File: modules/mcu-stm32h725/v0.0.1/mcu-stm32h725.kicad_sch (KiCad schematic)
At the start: 38 parts, among them J1 USB-C, J2 Side A, J3 Side B, U1 USB6B1RL, U2 TLV62569DBVR, U3 STM32H725RGV3, U4 TPS2116DRLR, Y1 25MHz

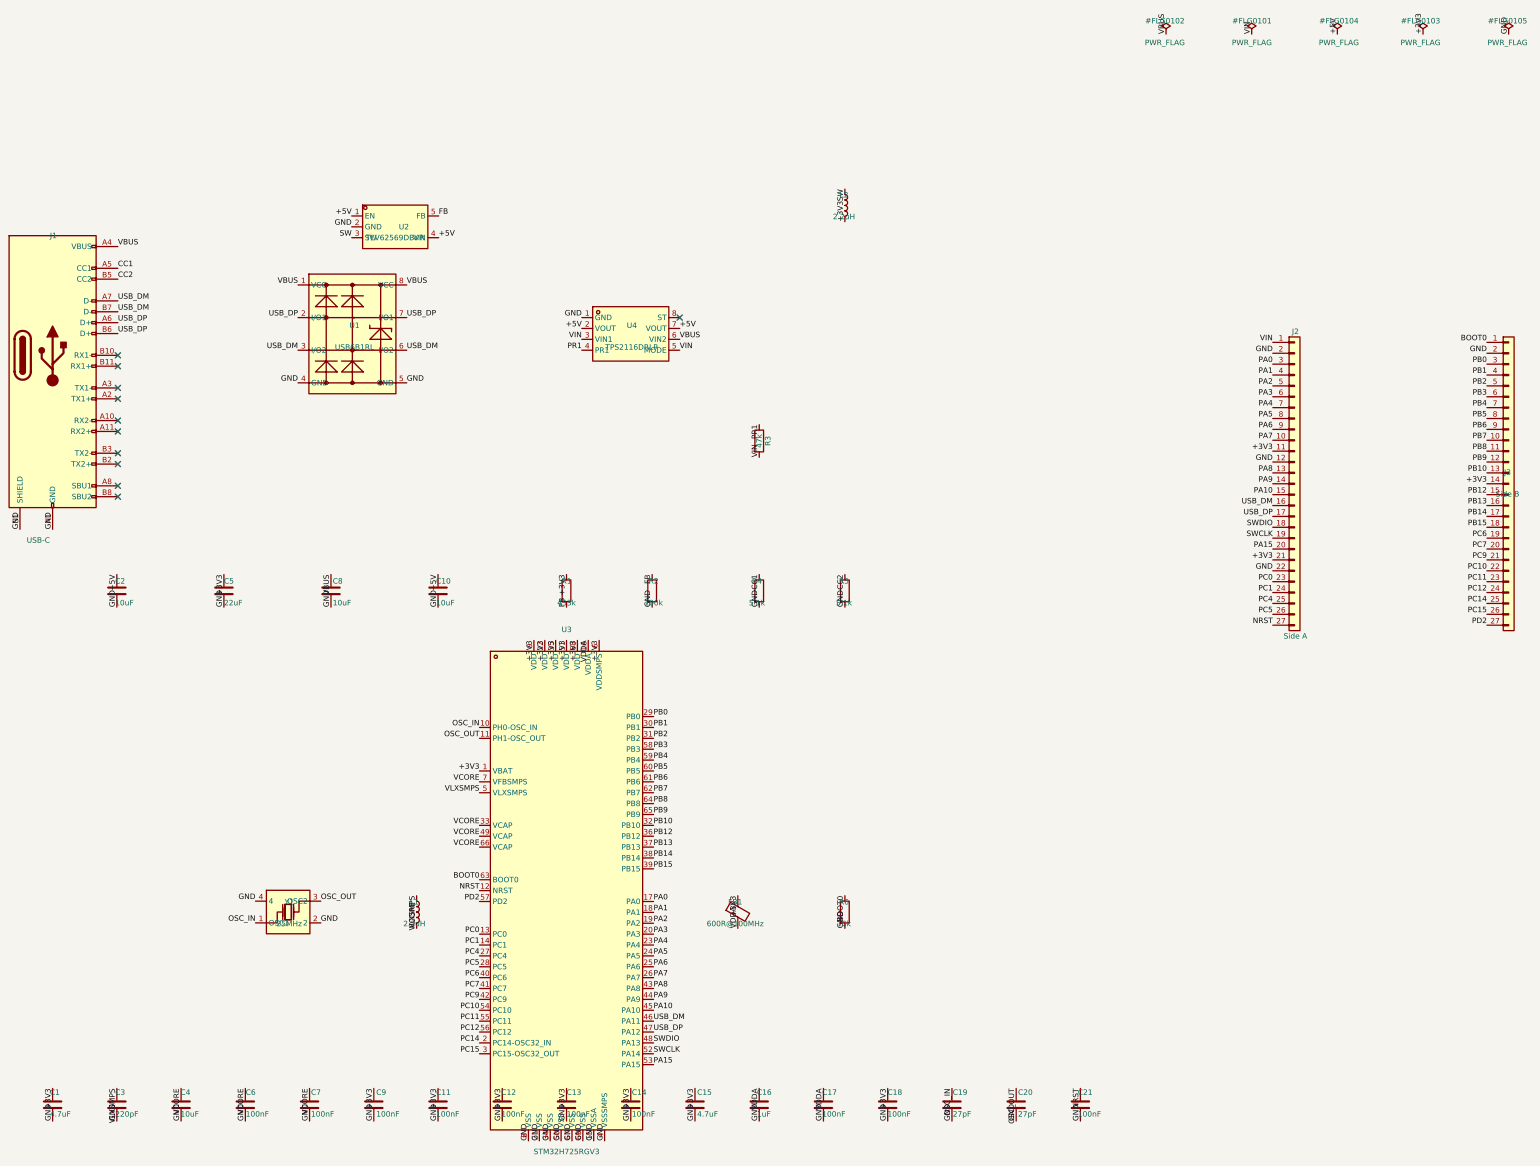
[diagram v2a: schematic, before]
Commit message: Lay out mcu-stm32h725 PCB: centered placement + 4-layer planes + optimal pin map
All 38 footprints placed (MCU centered for balanced GPIO fan-out; power block by USB-C; decoupling ringing the MCU; bulk caps right). GND plane (In1.Cu) + +3V3 plane (In2.Cu) zones added + filled. Castellation pads marked pad_prop_castellated in board + library (clears edge-clearance DRC). Schematic fixes: L1 footprint L_1210_3225Metric; USB-C symbol -> USB_C_Receptacle_USB2.0_16P to match the 16-pad footprint; J1 instance annotation repaired. Castellation pin map is crossing-free per edge and optimal for the centered MCU (~656mm ratsnest). DRC: 0 electrical violations (only unrouted nets + cosmetic silk/fill remain). Routing pending.

Co-Authored-By: Claude Opus 4.8 <noreply@anthropic.com>
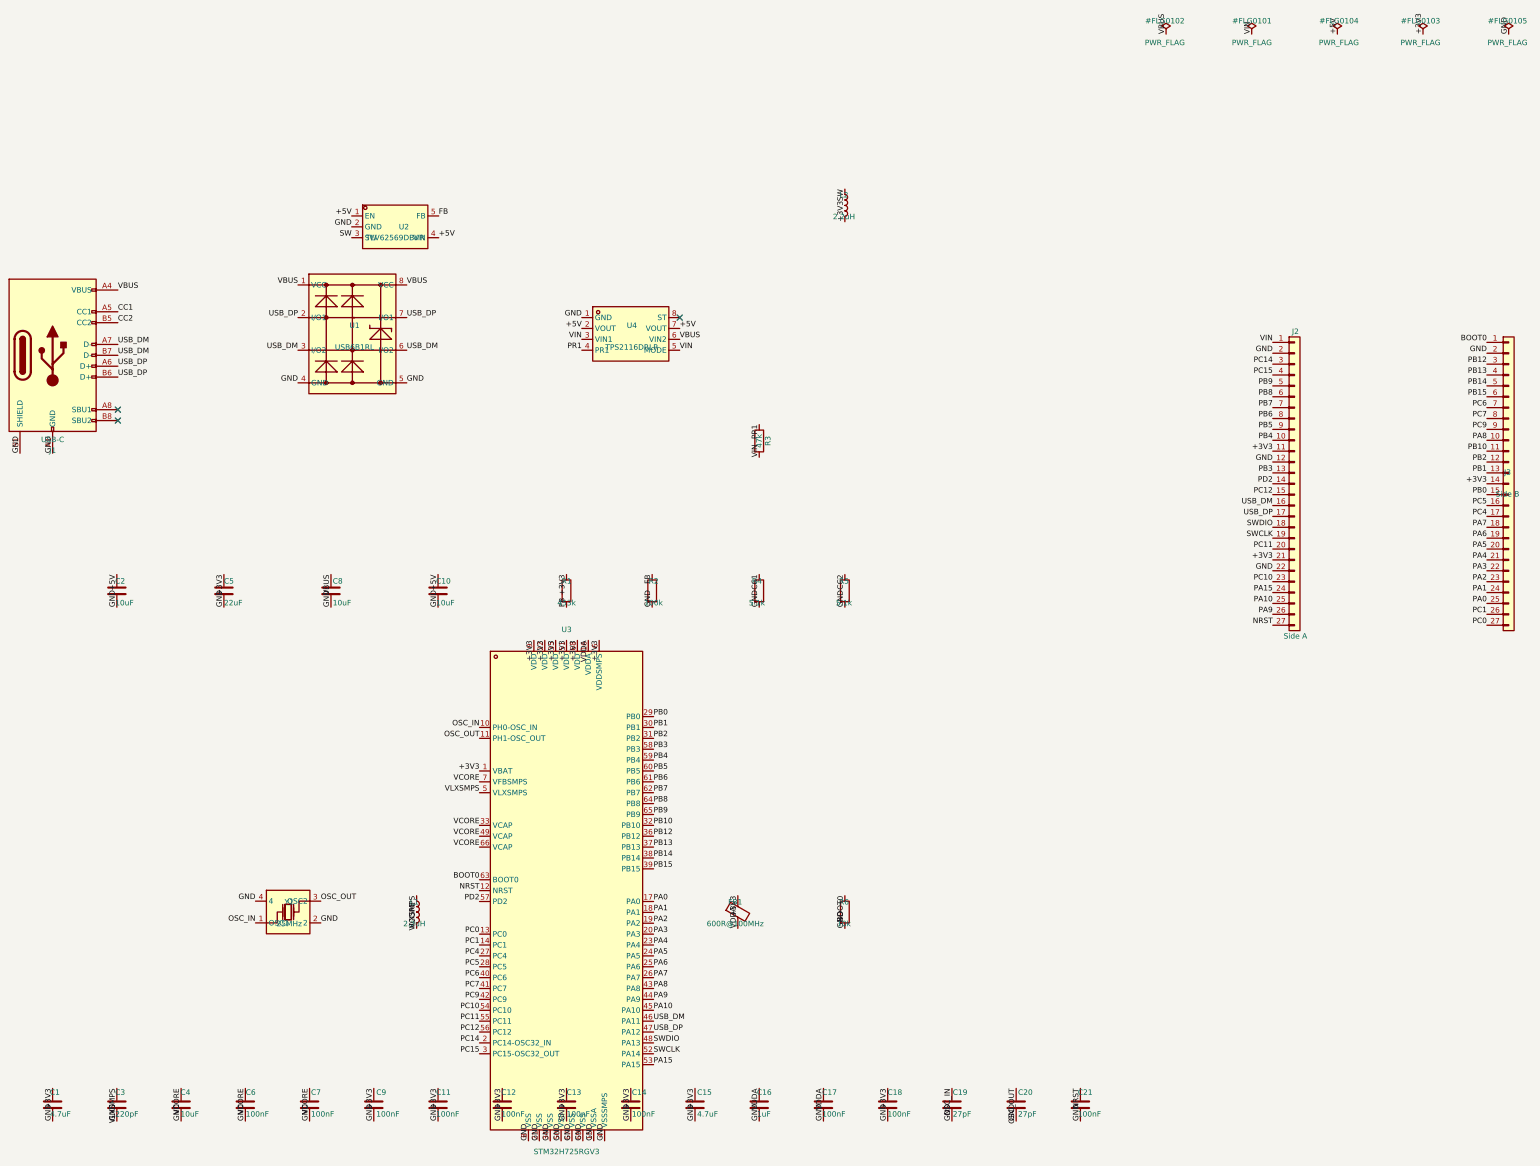
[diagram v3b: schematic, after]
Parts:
- removed J1: USB-C, mcu-stm32h725:USB-C_HYP_TC020-24LB02R_C23376530, symbol Connector:USB_C_Receptacle
- added J1: USB-C, mcu-stm32h725:USB-C_HYP_TC020-24LB02R_C23376530, symbol Connector:USB_C_Receptacle_USB2.0_16P
- L1: footprint Inductor_SMD:L_2520_2520Metric -> Inductor_SMD:L_1210_3225Metric
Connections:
- net CC1: now also J1.A5 (CC1)
- net CC2: now also J1.B5 (CC2)
- net GND: now also J1.A1 (GND), J1.A12 (GND), J1.B1 (GND), J1.B12 (GND), J1.S1 (SHIELD)
- net PA0: now also J3.25 (Pin_25); no longer J2.3 (Pin_3)
- net PA1: now also J3.24 (Pin_24); no longer J2.4 (Pin_4)
- net PA10: now also J2.25 (Pin_25); no longer J2.15 (Pin_15)
- net PA15: now also J2.24 (Pin_24); no longer J2.20 (Pin_20)
- net PA2: now also J3.23 (Pin_23); no longer J2.5 (Pin_5)
- net PA3: now also J3.22 (Pin_22); no longer J2.6 (Pin_6)
- net PA4: now also J3.21 (Pin_21); no longer J2.7 (Pin_7)
- net PA5: now also J3.20 (Pin_20); no longer J2.8 (Pin_8)
- net PA6: now also J3.19 (Pin_19); no longer J2.9 (Pin_9)
- net PA7: now also J3.18 (Pin_18); no longer J2.10 (Pin_10)
- net PA8: now also J3.10 (Pin_10); no longer J2.13 (Pin_13)
- net PA9: now also J2.26 (Pin_26); no longer J2.14 (Pin_14)
- net PB0: now also J3.15 (Pin_15); no longer J3.3 (Pin_3)
- net PB1: now also J3.13 (Pin_13); no longer J3.4 (Pin_4)
- net PB10: now also J3.11 (Pin_11); no longer J3.13 (Pin_13)
- net PB12: now also J3.3 (Pin_3); no longer J3.15 (Pin_15)
- net PB13: now also J3.4 (Pin_4); no longer J3.16 (Pin_16)
- net PB14: now also J3.5 (Pin_5); no longer J3.17 (Pin_17)
- net PB15: now also J3.6 (Pin_6); no longer J3.18 (Pin_18)
- net PB2: now also J3.12 (Pin_12); no longer J3.5 (Pin_5)
- net PB3: now also J2.13 (Pin_13); no longer J3.6 (Pin_6)
- net PB4: now also J2.10 (Pin_10); no longer J3.7 (Pin_7)
- net PB5: now also J2.9 (Pin_9); no longer J3.8 (Pin_8)
- net PB6: now also J2.8 (Pin_8); no longer J3.9 (Pin_9)
- net PB7: now also J2.7 (Pin_7); no longer J3.10 (Pin_10)
- net PB8: now also J2.6 (Pin_6); no longer J3.11 (Pin_11)
- net PB9: now also J2.5 (Pin_5); no longer J3.12 (Pin_12)
- net PC0: now also J3.27 (Pin_27); no longer J2.23 (Pin_23)
- net PC1: now also J3.26 (Pin_26); no longer J2.24 (Pin_24)
- net PC10: now also J2.23 (Pin_23); no longer J3.22 (Pin_22)
- net PC11: now also J2.20 (Pin_20); no longer J3.23 (Pin_23)
- net PC12: now also J2.15 (Pin_15); no longer J3.24 (Pin_24)
- net PC14: now also J2.3 (Pin_3); no longer J3.25 (Pin_25)
- net PC15: now also J2.4 (Pin_4); no longer J3.26 (Pin_26)
- net PC4: now also J3.17 (Pin_17); no longer J2.25 (Pin_25)
- net PC5: now also J3.16 (Pin_16); no longer J2.26 (Pin_26)
- net PC6: now also J3.7 (Pin_7); no longer J3.19 (Pin_19)
- net PC7: now also J3.8 (Pin_8); no longer J3.20 (Pin_20)
- net PC9: now also J3.9 (Pin_9); no longer J3.21 (Pin_21)
- net PD2: now also J2.14 (Pin_14); no longer J3.27 (Pin_27)
- net USB_DM: now also J1.A7 (D-), J1.B7 (D-)
- net USB_DP: now also J1.A6 (D+), J1.B6 (D+)
- net VBUS: now also J1.A4 (VBUS), J1.A9 (VBUS), J1.B4 (VBUS), J1.B9 (VBUS)
- no-connect marks 11 -> 3
